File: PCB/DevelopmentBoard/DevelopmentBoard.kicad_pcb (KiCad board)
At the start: 2 copper layers, 128.3 x 64.8 mm, 37 parts, among them IC1 FE1.1S_USB_Controller, J1 Conn_01x04_MountingPin, J2 USB-A, J3 USB-A, J4 CRJ007_RJ45, U1 Pi_CM4, U2 Barometer_Grove, U3 D24V22F5, U4 Micro-USB, U5 VN-100_Breakout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

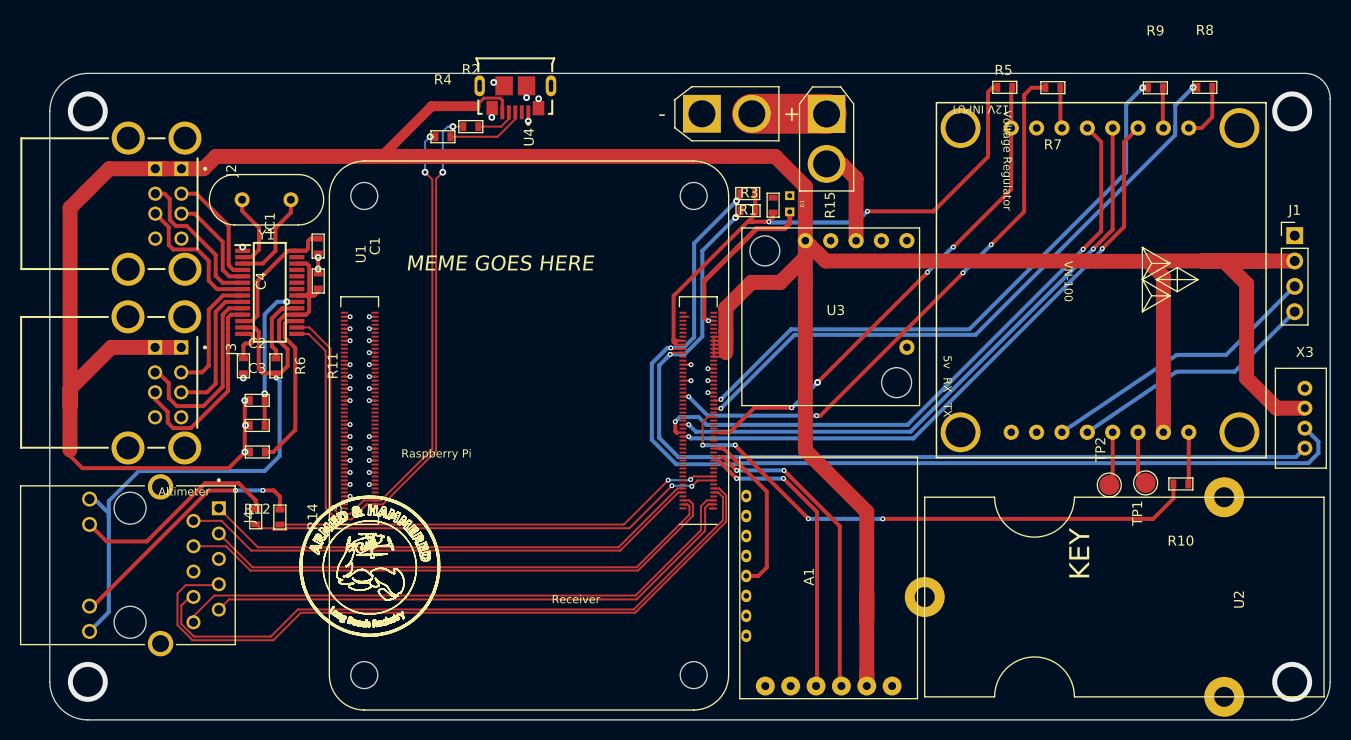
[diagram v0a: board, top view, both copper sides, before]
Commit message: Trace matched Micro USB
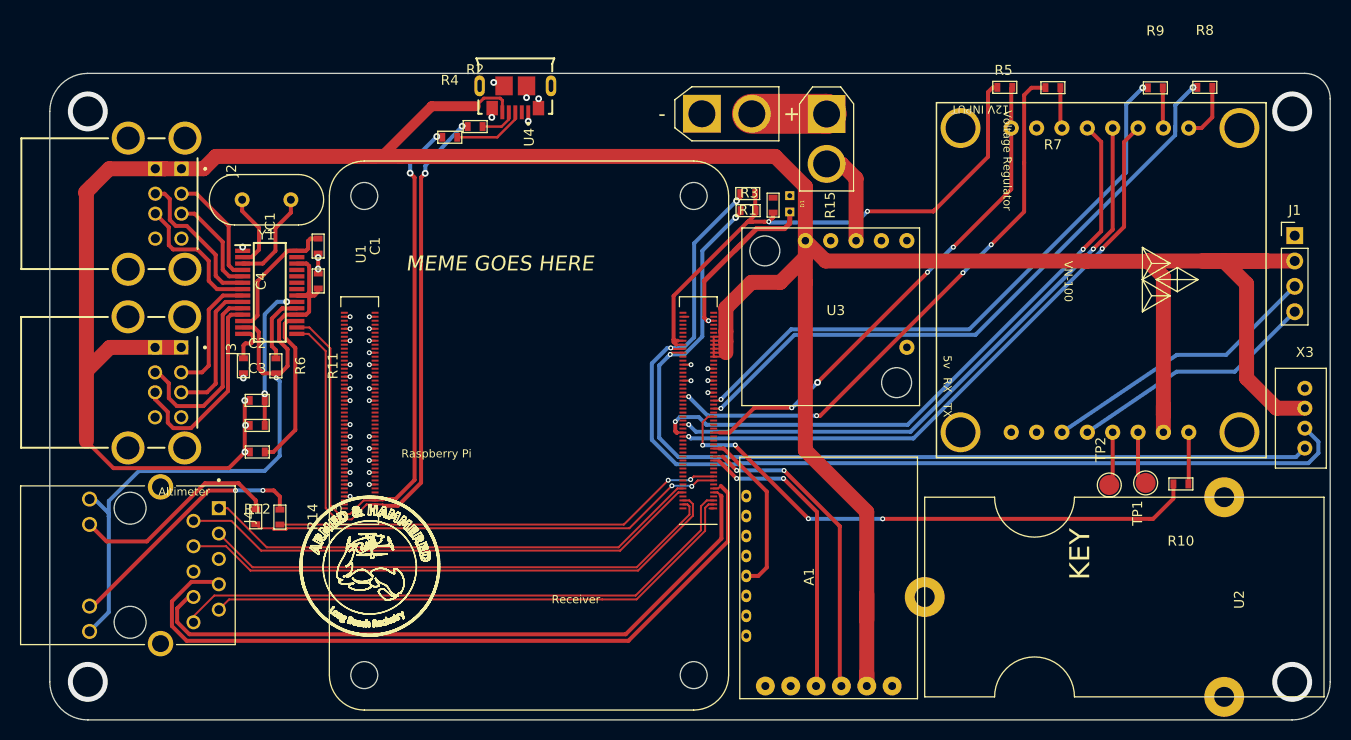
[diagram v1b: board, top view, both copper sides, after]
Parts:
- moved R4 0.69 mm to (132.5, 72.2)
- moved R2 0.43 mm to (135.1, 71.1)
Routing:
- net /ETH_P2_P: track 72.4 -> 75.3 mm
- net +5V: track 336.4 -> 334.3 mm
- net /ETH_P2_N: track 66.5 -> 68.0 mm
- net /D0+: track 65.8 -> 67.0 mm
- net Net-(R4-Pad2): track 7.92 -> 7.25 mm
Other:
- net class D0 added: clearance 0.127, trace_width 0.4, via_dia 0.6858, via_drill 0.3302
- net class ETH_P2 added: clearance 0.127, trace_width 0.4, via_dia 0.6858, via_drill 0.3302
- net class USB Data removed

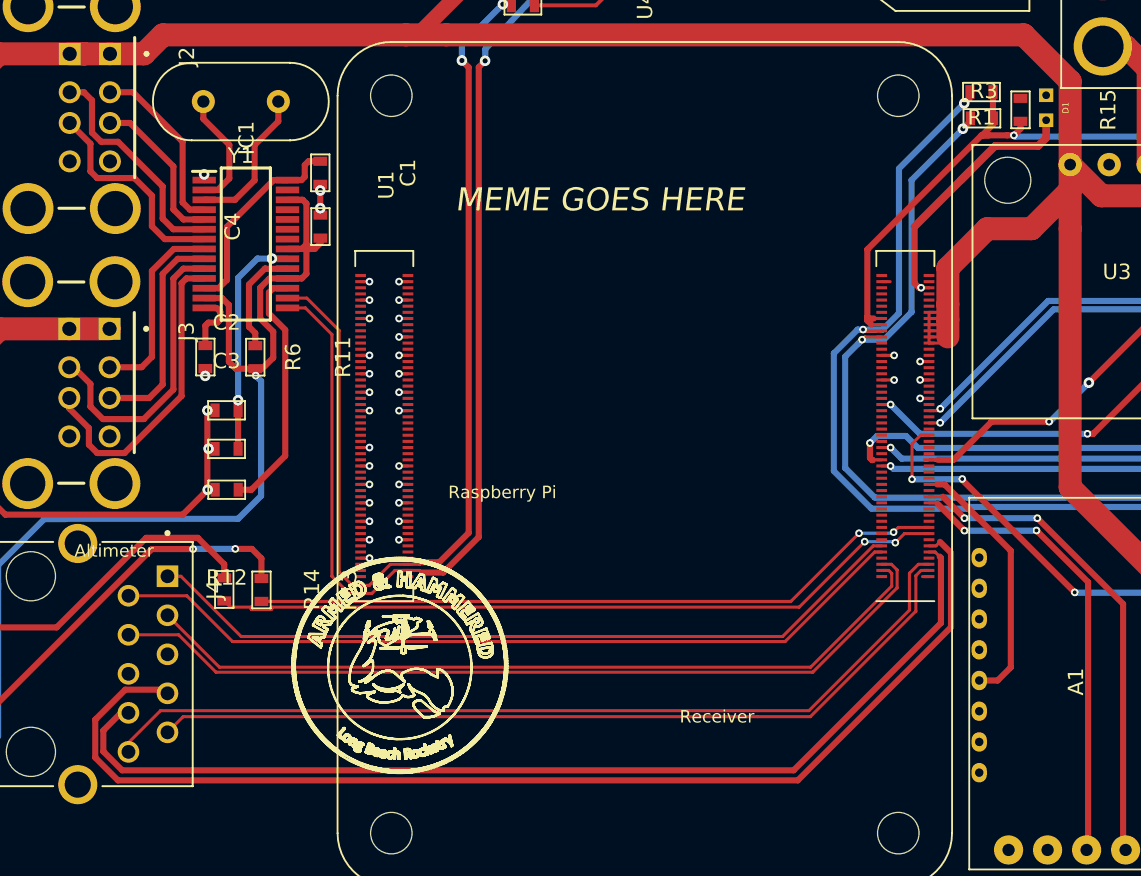
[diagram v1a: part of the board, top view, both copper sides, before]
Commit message: Trace matched Second pair ethernet
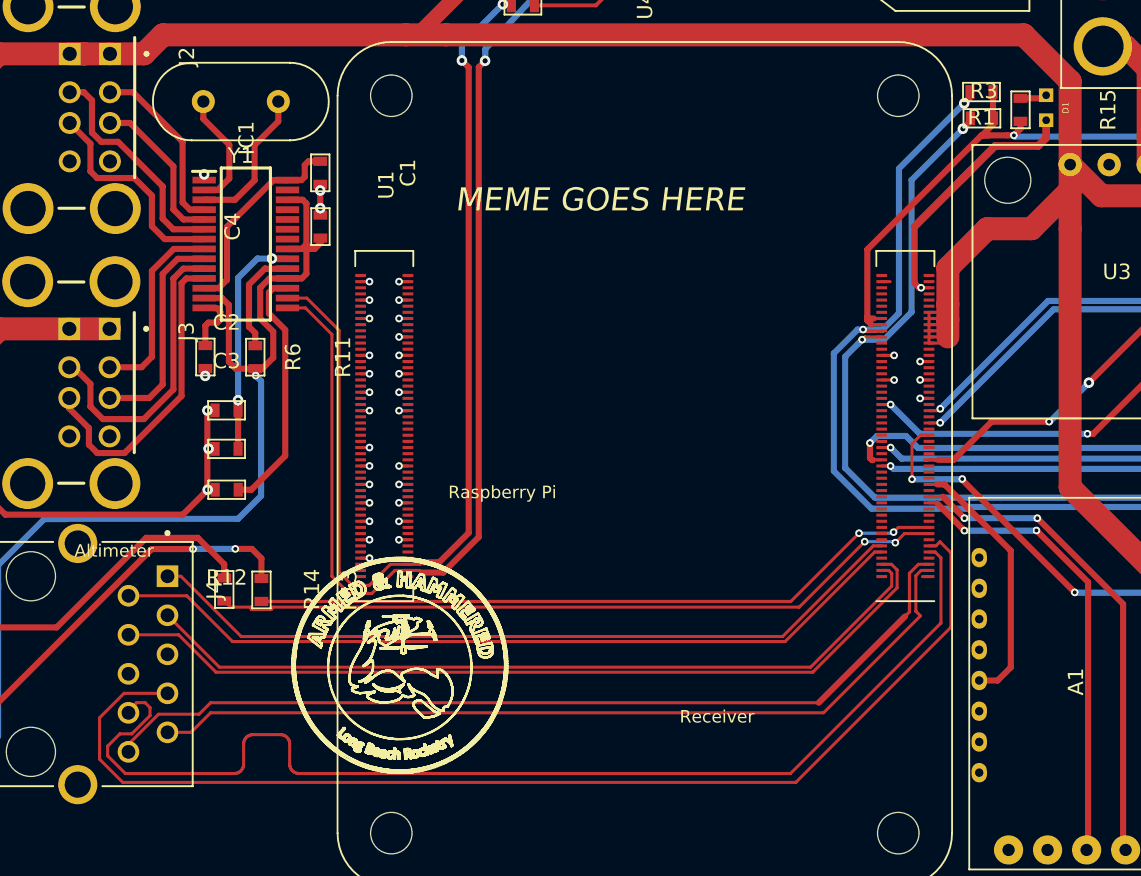
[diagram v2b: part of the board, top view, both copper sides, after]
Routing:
- net /ETH_P2_N: track 68.0 -> 75.1 mm
- net Net-(D1-Pad2): track 0.00 -> 1.75 mm
- net /ETH_P3_P: track 55.3 -> 55.9 mm
- net /ETH_P3_N: track 59.0 -> 59.6 mm
- net /ETH_P2_P: track 75.3 -> 74.8 mm
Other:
- net class ETH_P3 added: clearance 0.127, trace_width 0.4, via_dia 0.6858, via_drill 0.3302

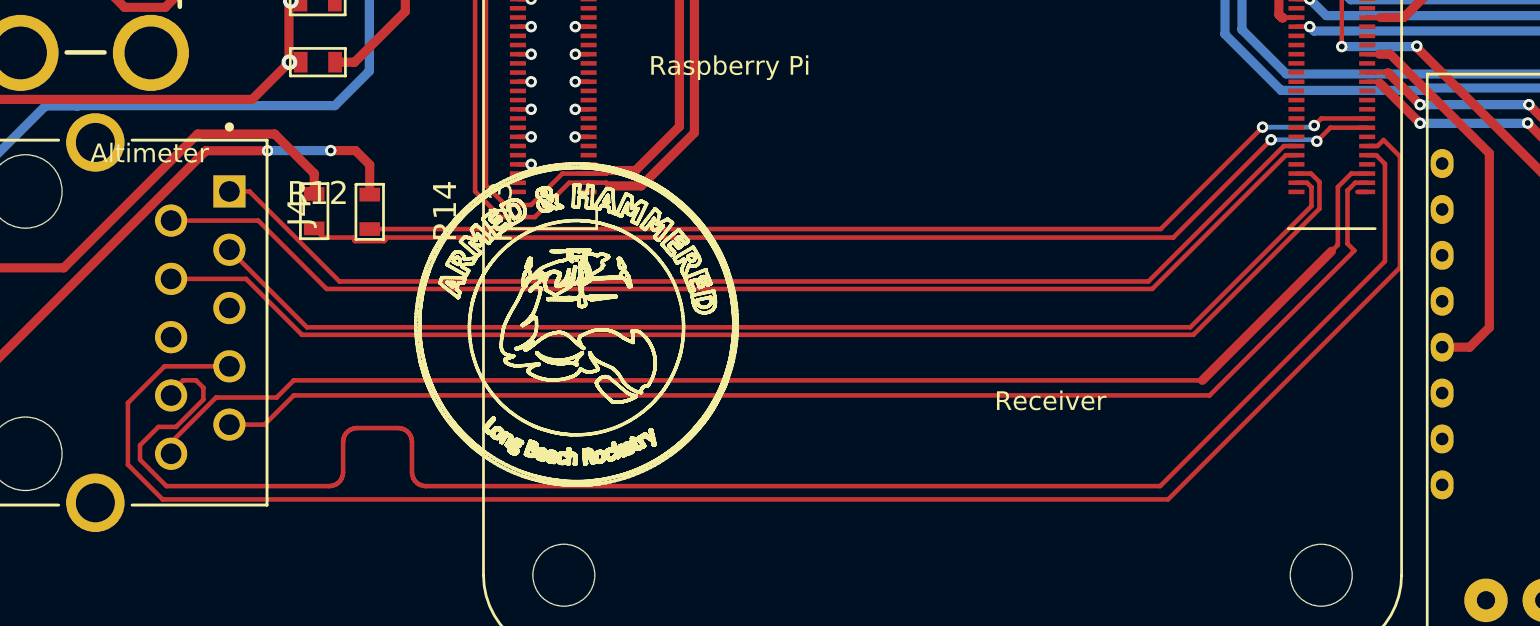
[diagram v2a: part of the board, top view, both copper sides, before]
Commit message: Ethernet Trace Matching
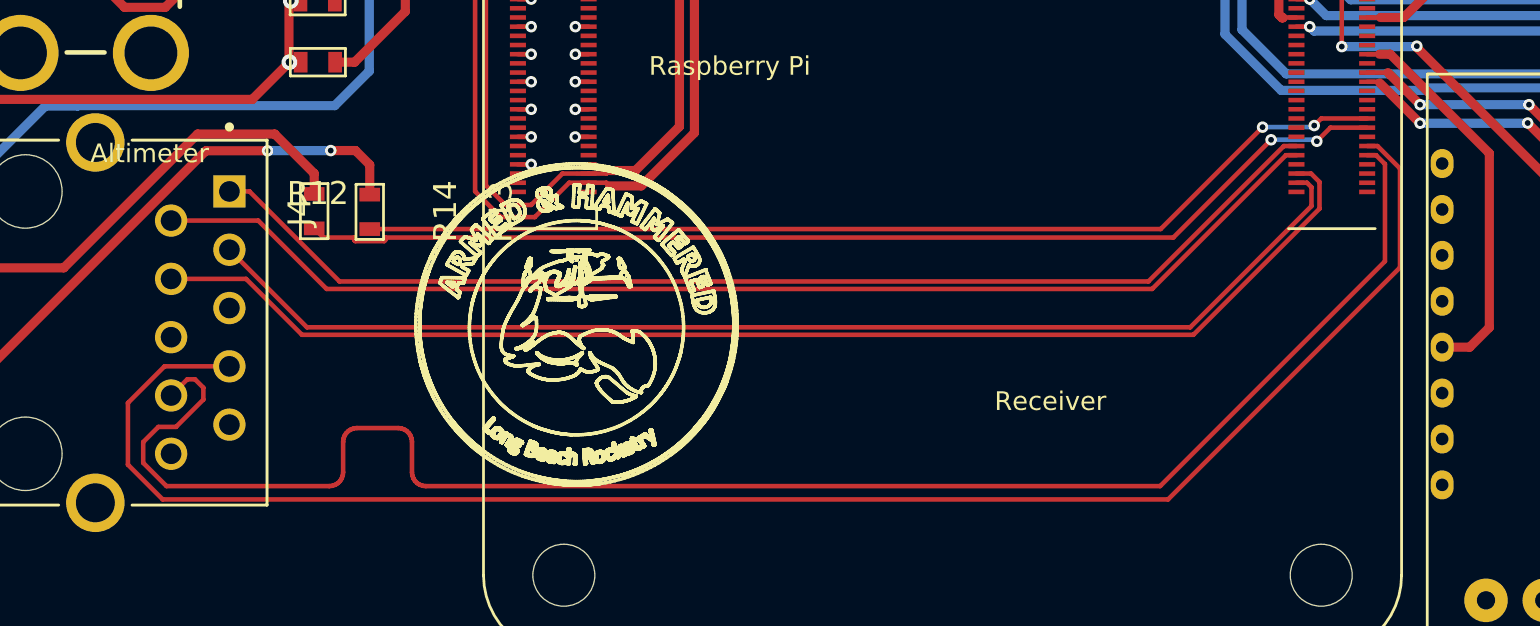
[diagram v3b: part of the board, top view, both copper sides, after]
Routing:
- net /ETH_P3_N: track 59.6 -> 1.06 mm
- net /ETH_P3_P: track 55.9 -> 0.45 mm
- net /ETH_P2_P: track 74.8 -> 74.3 mm
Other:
- net class ETH_P2: trace_width 0.4 -> 0.2
- net class ETH_P3: trace_width 0.4 -> 0.2

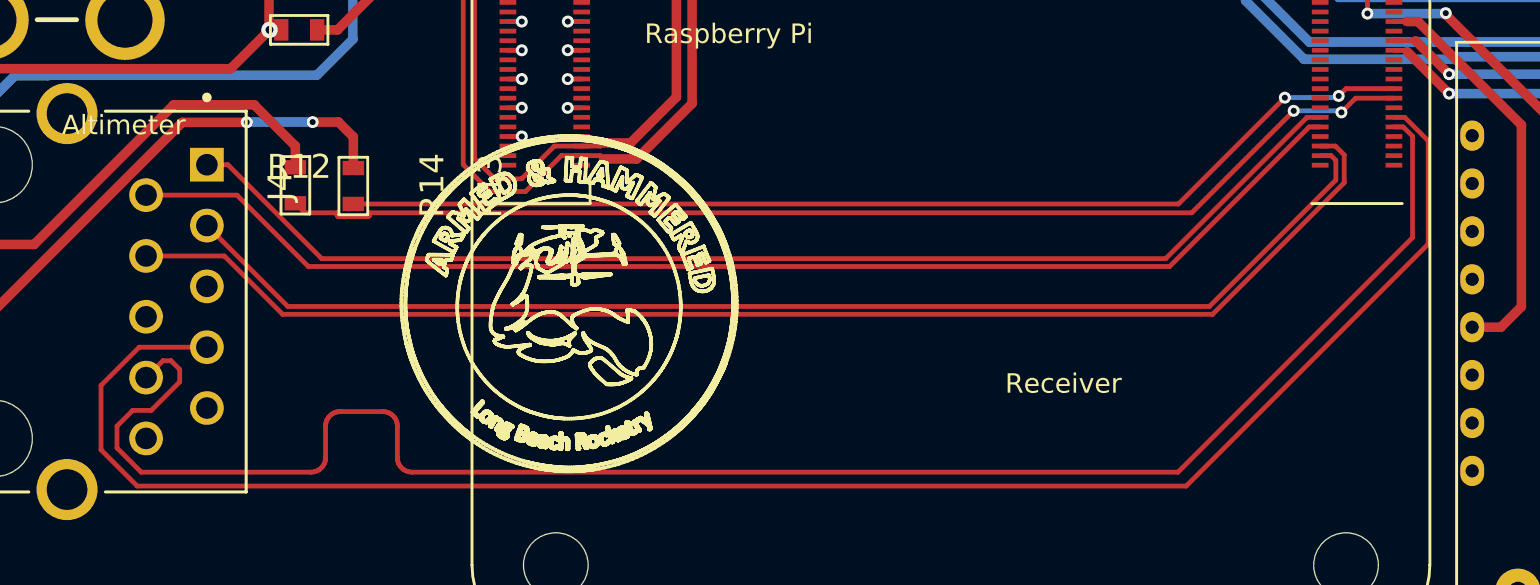
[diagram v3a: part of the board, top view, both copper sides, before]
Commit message: Made more differential pairs the same
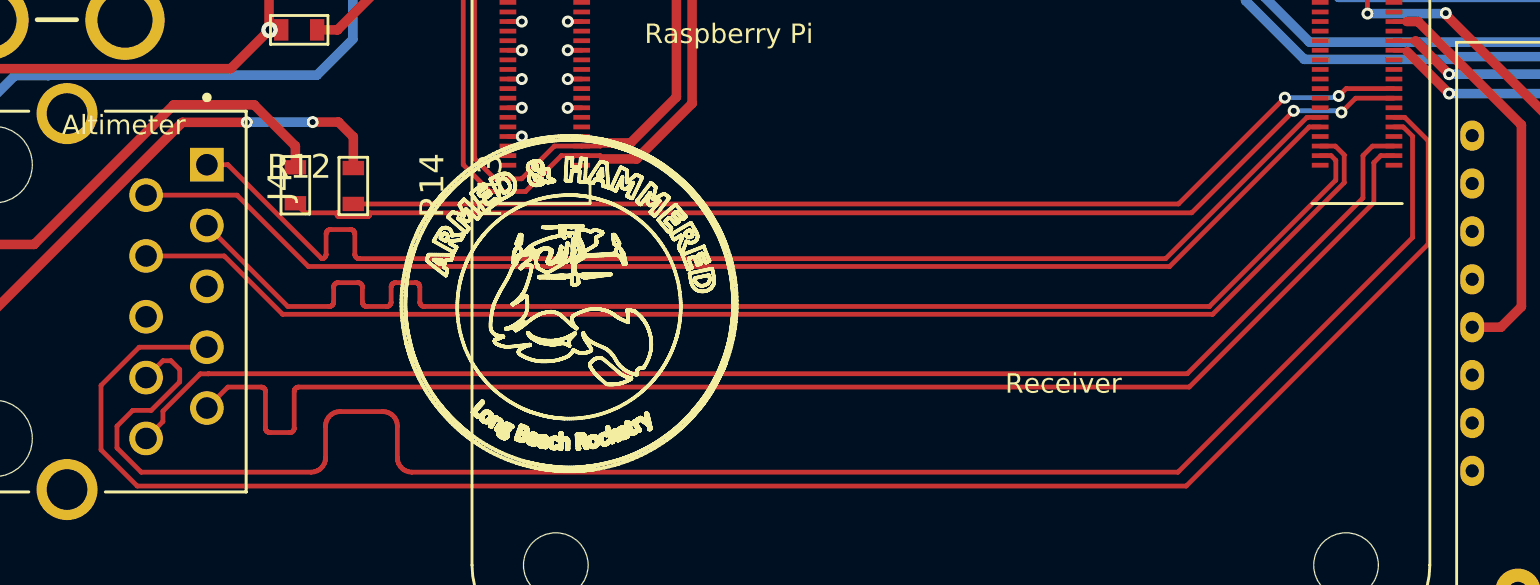
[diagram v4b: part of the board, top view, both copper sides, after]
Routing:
- net /ETH_P3_N: track 1.06 -> 59.5 mm
- net /ETH_P3_P: track 0.45 -> 58.8 mm
- net /ETH_P1_P: track 52.3 -> 55.6 mm
- net /ETH_P0_P: track 50.6 -> 52.7 mm

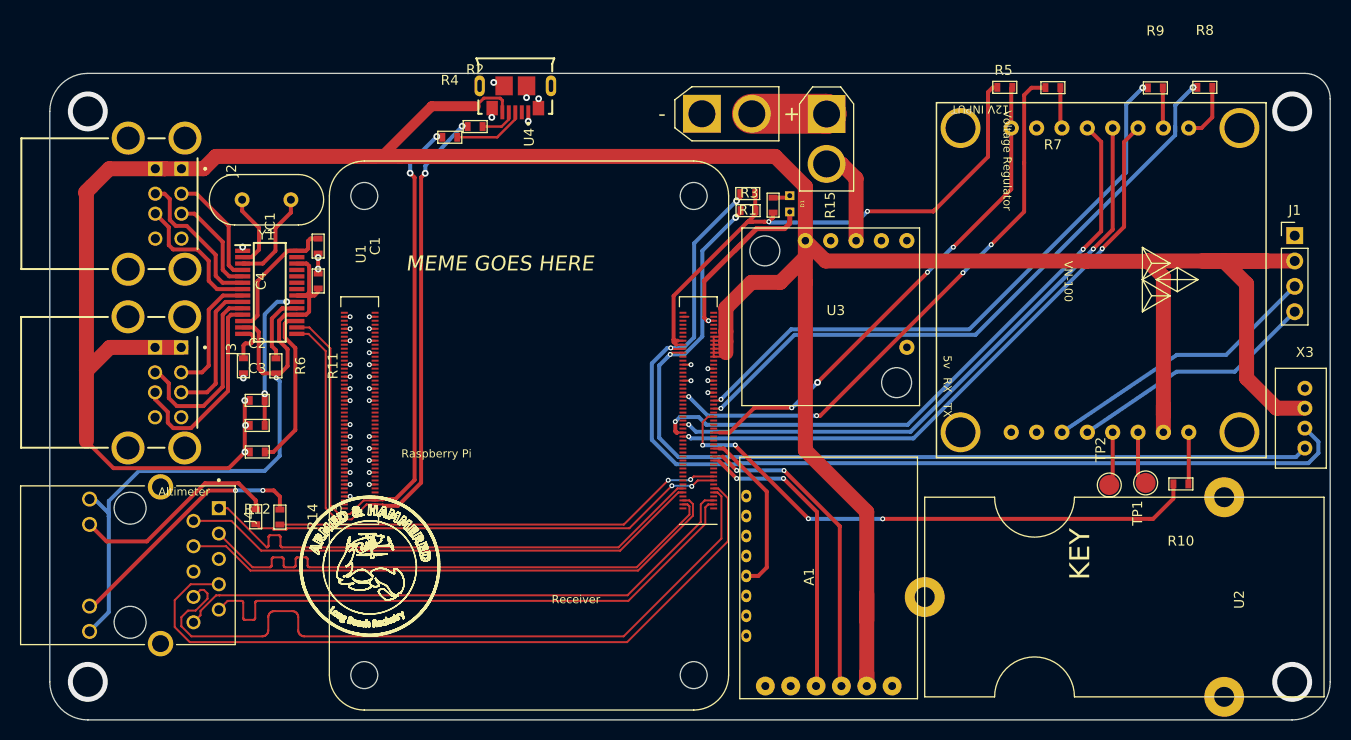
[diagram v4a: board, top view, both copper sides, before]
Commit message: Adjusted ethernet pair lengths
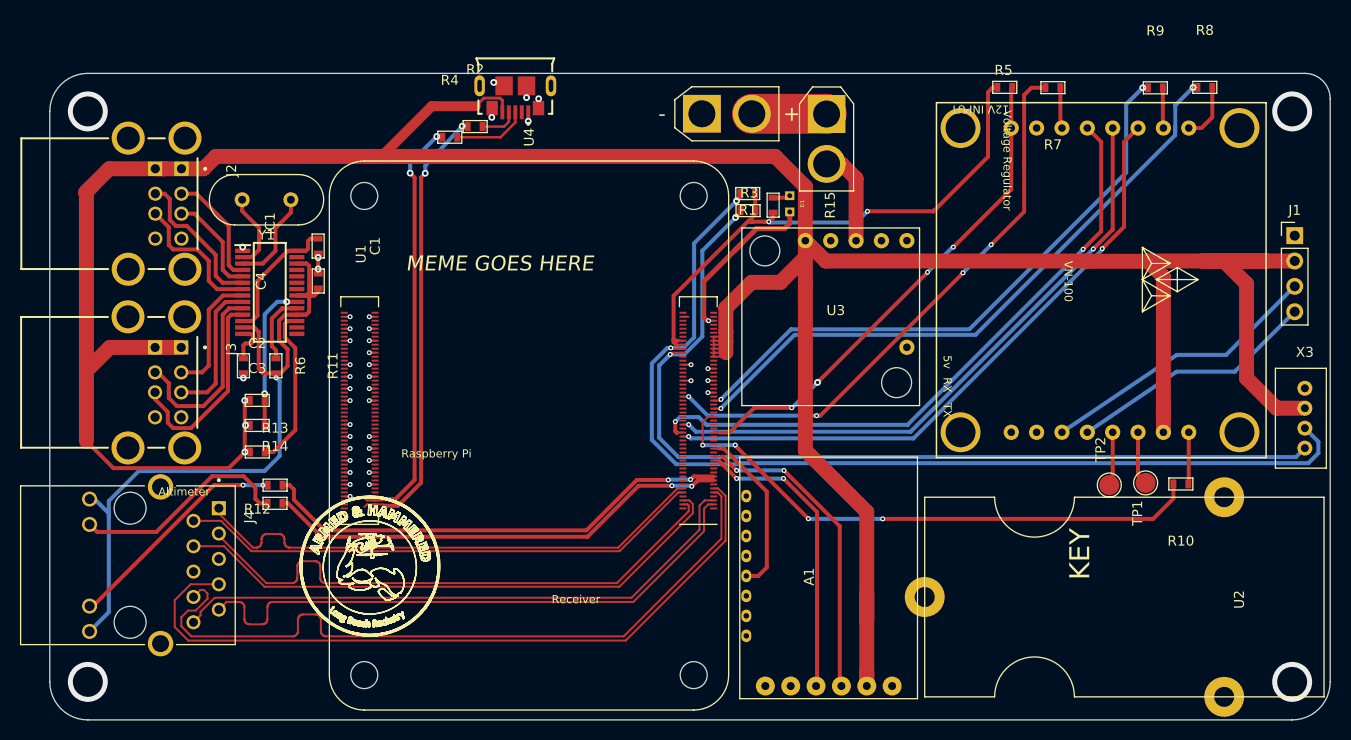
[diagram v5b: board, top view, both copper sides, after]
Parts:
- moved R13 3.24 mm to (115.0, 107.0), turned to 0 degrees
- moved R14 2.36 mm to (115.0, 108.9), turned to 0 degrees
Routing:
- net /D0+: track 67.0 -> 42.8 mm
- net /D0-: track 68.9 -> 45.2 mm
- net Net-(J4-Pad13): track 25.4 -> 22.9 mm
- net /ETH_LEDG: track 45.5 -> 47.9 mm
- net /ETH_LEDY: track 48.3 -> 47.0 mm
- net /ETH_P1_P: track 55.6 -> 56.9 mm
- net /ETH_P1_N: track 55.6 -> 56.8 mm
- net Net-(J4-Pad12): track 21.4 -> 22.2 mm
- net /ETH_P2_N: track 74.9 -> 74.4 mm
- net /ETH_P2_P: track 74.3 -> 73.8 mm
